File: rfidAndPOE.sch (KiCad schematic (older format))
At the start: 0 parts

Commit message: Added a few more components to the library and got about halfway done with the PoE power supply section.
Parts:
- added C1: 0.1uF, 100V, X7R, symbol C
- added C2: 1uF, 100V, symbol C
- added C3: 68pF, 200V, symbol C
- added C4: 4.7uF, 10V, symbol C
- added C5: 4.7uF, 100v, symbol CP1
- added D2: SMAJ58A, symbol DIODESCH
- added D3: BAS516, symbol DIODE
- added D5: 1N5237B, 8.2V, symbol DIODESCH
- added D? (x2): CDNBS04-B08200, symbol CDNBS04-B08200
- added L1: 3.3uH, symbol INDUCTOR
- added Q1: Si3440DV, NFET, symbol MOSFET_N
- added Q2: MMBTA42, symbol NPN
- added R2, R3: 220K, symbol R
- added R4, R400: 0.250R, symbol R
- added R5: 4.7K, symbol R
- added R6: 510R, symbol R
- added R7: 100R, 1/8W, symbol R
- added T?: PA1134, symbol PA1134
- added U?: LTC4267-3, symbol LTC4267-3
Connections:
- net labels added: GNDA
- wire segments 0 -> 61
- no-connect marks 0 -> 1

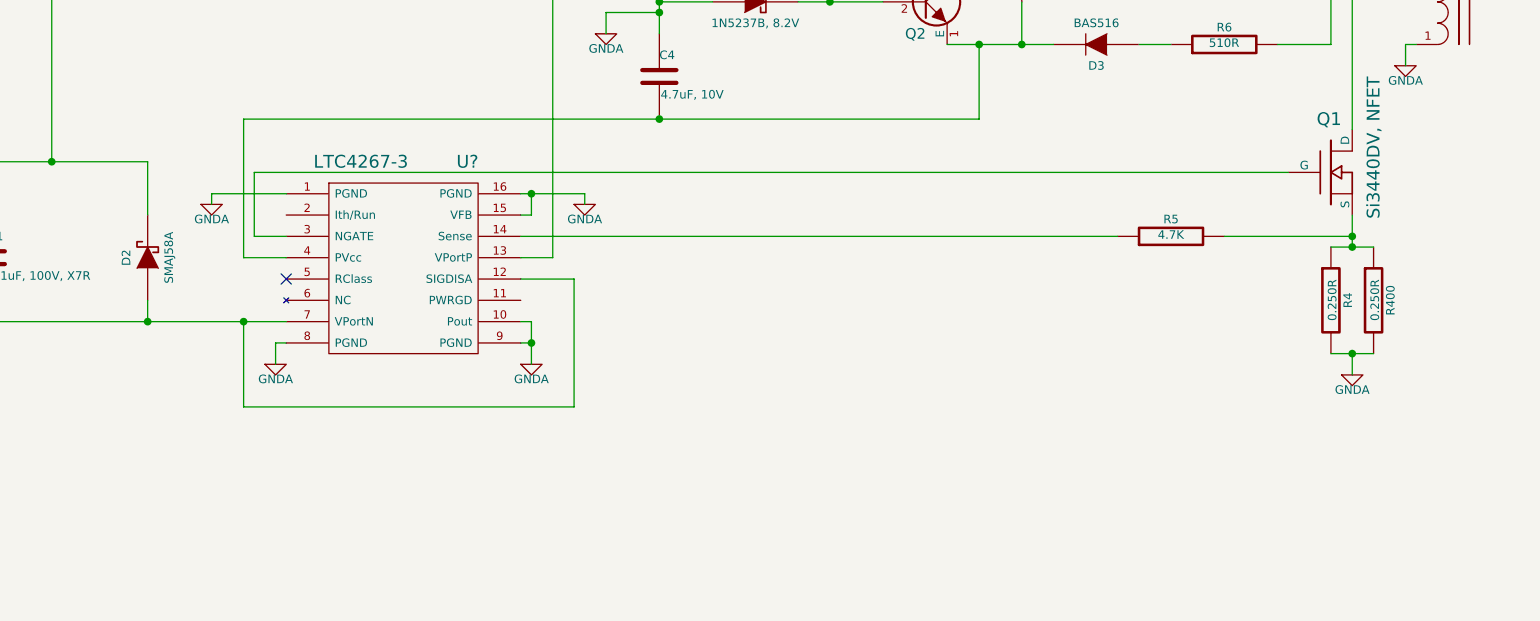
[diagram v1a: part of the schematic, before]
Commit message: PoE schematic done up to the isolation point.
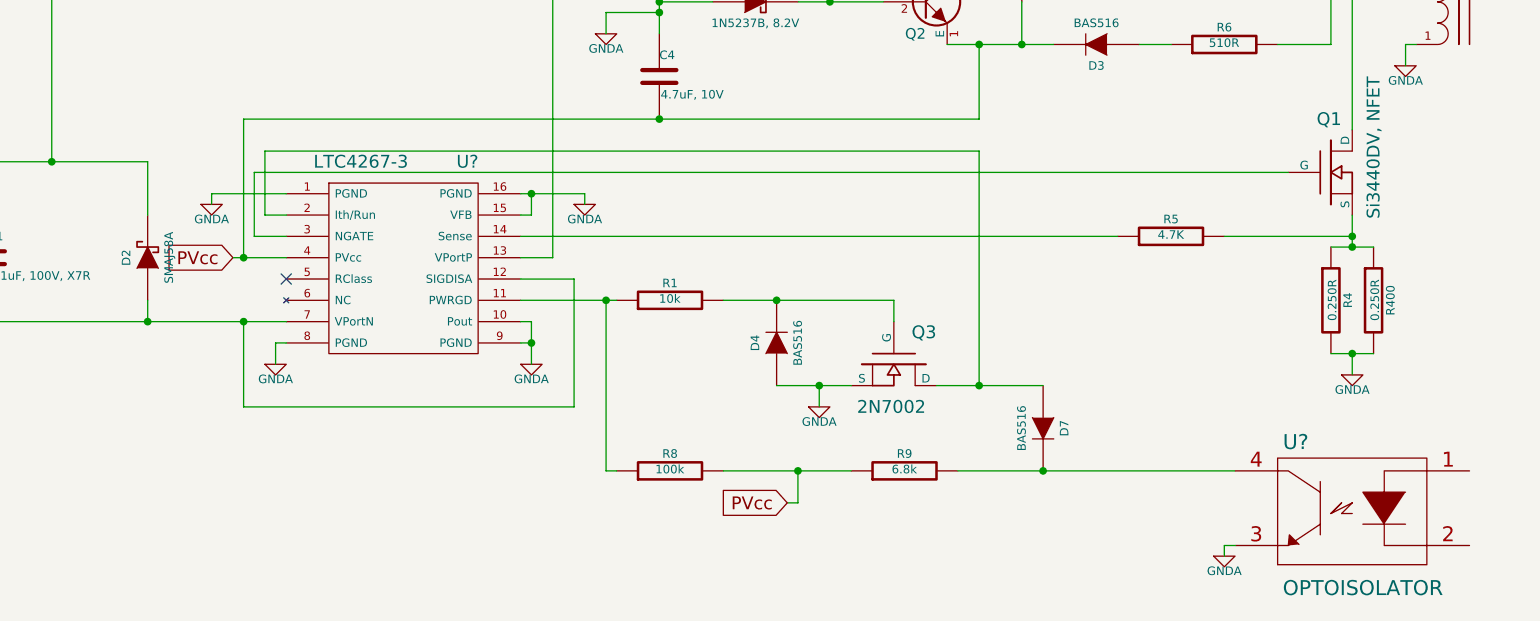
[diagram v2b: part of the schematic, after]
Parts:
- added D4, D7: BAS516, symbol DIODE
- added Q3: 2N7002, symbol MOSFET_N
- added R1: 10k, symbol R
- added R8: 100k, symbol R
- added R9: 6.8k, symbol R
- added U?: OPTOISOLATOR, symbol OPTOISOLATOR
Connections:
- net labels added: PVcc
- wire segments 61 -> 79
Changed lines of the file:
@@
 LIBS:valves
 LIBS:rfid
+LIBS:rfidAndPOE-cache
 EELAYER 24 0
 EELAYER END
@@
 	5400 3900 5400 4550
 Wire Wire Line
-	5400 4550 5600 4550
+	5350 4550 5600 4550
 $Comp
 L DIODESCH D5
@@
 	5250 4250 5600 4250
 NoConn ~ 5600 4650
+$Comp
+L MOSFET_N Q3
+U 1 1 529FE736
+P 8450 5050
+F 0 "Q3" V 8300 5250 60  0000 R CNN
+F 1 "2N7002" V 8650 5200 60  0000 R CNN
+F 2 "" H 8450 5050 60  0000 C CNN
+F 3 "" H 8450 5050 60  0000 C CNN
+	1    8450 5050
+	0    1    1    0
+$EndComp
+$Comp
+L DIODE D7
+U 1 1 529FE790
+P 9150 5350
+F 0 "D7" H 9150 5450 40  0000 C CNN
+F 1 "BAS516" H 9150 5250 40  0000 C CNN
+F 2 "" H 9150 5350 60  0000 C CNN
+F 3 "" H 9150 5350 60  0000 C CNN
+	1    9150 5350
+	0    1    1    0
+$EndComp
+$Comp
+L DIODE D4
+U 1 1 529FE7EB
+P 7900 4950
+F 0 "D4" H 7900 5050 40  0000 C CNN
+F 1 "BAS516" H 7900 4850 40  0000 C CNN
+F 2 "" H 7900 4950 60  0000 C CNN
+F 3 "" H 7900 4950 60  0000 C CNN
+	1    7900 4950
+	0    -1   -1   0
+$EndComp
+Wire Wire Line
+	8450 4750 8450 4850
+Wire Wire Line
+	7650 4750 8450 4750
+Wire Wire Line
+	7900 5150 8250 5150
+$Comp
+L GNDA #PWR?
+U 1 1 529FE8B5
+P 8100 5250
+F 0 "#PWR?" H 8100 5250 40  0001 C CNN
+F 1 "GNDA" H 8100 5180 40  0000 C CNN
+F 2 "" H 8100 5250 60  0000 C CNN
+F 3 "" H 8100 5250 60  0000 C CNN
+	1    8100 5250
+	1    0    0    -1
+$EndComp
+Wire Wire Line
+	8100 5150 8100 5250
+Connection ~ 8100 5150
+$Comp
+L R R1
+U 1 1 529FE931
+P 7400 4750
+F 0 "R1" V 7480 4750 40  0000 C CNN
+F 1 "10k" V 7407 4751 40  0000 C CNN
+F 2 "" V 7330 4750 30  0000 C CNN
+F 3 "" H 7400 4750 30  0000 C CNN
+	1    7400 4750
+	0    -1   -1   0
+$EndComp
+$Comp
+L R R8
+U 1 1 529FE945
+P 7400 5550
+F 0 "R8" V 7480 5550 40  0000 C CNN
+F 1 "100k" V 7407 5551 40  0000 C CNN
+F 2 "" V 7330 5550 30  0000 C CNN
+F 3 "" H 7400 5550 30  0000 C CNN
+	1    7400 5550
+	0    -1   -1   0
+$EndComp
+$Comp
+L R R9
+U 1 1 529FE959
+P 8500 5550
+F 0 "R9" V 8580 5550 40  0000 C CNN
+F 1 "6.8k" V 8507 5551 40  0000 C CNN
+F 2 "" V 8430 5550 30  0000 C CNN
+F 3 "" H 8500 5550 30  0000 C CNN
+	1    8500 5550
+	0    -1   -1   0
+$EndComp
+Wire Wire Line
+	6700 4750 7150 4750
+Connection ~ 7900 4750
+Wire Wire Line
+	7100 4750 7100 5550
+Wire Wire Line
+	7100 5550 7150 5550
+Connection ~ 7100 4750
+Wire Wire Line
+	7650 5550 8250 5550
+Wire Wire Line
+	8750 5550 10050 5550
+Wire Wire Line
+	8650 5150 9150 5150
+Wire Wire Line
+	5600 4350 5500 4350
+Wire Wire Line
+	5500 4350 5500 4050
+Wire Wire Line
+	5500 4050 8850 4050
+Wire Wire Line
+	8850 4050 8850 5150
+Connection ~ 8850 5150
+Text GLabel 5350 4550 0    60   Input ~ 0
+PVcc
+Text GLabel 7950 5700 0    60   Input ~ 0
+PVcc
+Wire Wire Line
+	7950 5700 8000 5700
+Wire Wire Line
+	8000 5700 8000 5550
+Connection ~ 8000 5550
+Connection ~ 5400 4550
+$Comp
+L OPTOISOLATOR U?
+U 1 1 529FF254
+P 10000 5750
+F 0 "U?" H 10335 6085 70  0000 C CNN
+F 1 "OPTOISOLATOR" H 10650 5400 70  0000 C CNN
+F 2 "" H 10600 5750 60  0000 C CNN
+F 3 "" H 10600 5750 60  0000 C CNN
+	1    10000 5750
+	1    0    0    -1
+$EndComp
+Connection ~ 9150 5550
+$Comp
+L GNDA #PWR?
+U 1 1 529FF2D9
+P 10000 5950
+F 0 "#PWR?" H 10000 5950 40  0001 C CNN
+F 1 "GNDA" H 10000 5880 40  0000 C CNN
+F 2 "" H 10000 5950 60  0000 C CNN
+F 3 "" H 10000 5950 60  0000 C CNN
+	1    10000 5950
+	1    0    0    -1
+$EndComp
+Wire Wire Line
+	10050 5900 10000 5900
+Wire Wire Line
+	10000 5900 10000 5950
 $EndSCHEMATC

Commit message: Placed all of the components for the 5V isolated output from PoE.
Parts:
- added C14, C?: 100uF, 6.3V, X5R, symbol C
- added C6: 470pF, symbol C
- added C9: 220uF, 6.3v, symbol CP1
- added C? (x4): C, symbol C
- added D1: SMB540, symbol DIODESCH
- added D?: VREF, symbol VREF
- added R10: 10R, symbol R
- added R? (x5): R, symbol R
- U?: value OPTOISOLATOR -> PS2811
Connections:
- net labels added: 5VPoE, GND
- wire segments 79 -> 93

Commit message: Finished up the output side of the PoE 5V supply.
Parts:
- C12: renamed from C?; value C -> 1uF
- C13: renamed from C?; value C -> 33nF
- C7: renamed from C?; value C -> 27nF
- C8: renamed from C?; value C -> 2.8nF, 250VAC, YCAP
- D8: renamed from D?; value VREF -> TLV431
- R11: renamed from R?; value R -> 1k
- R12: renamed from R?; value R -> 47k
- R13: renamed from R?; value R -> 100k, 1%
- R14: renamed from R?; value R -> 33.2k
- R21: renamed from R?; value R -> 470R
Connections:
- wire segments 93 -> 112
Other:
- moved on the sheet: C12, C13, C7, C8, R11, R12, R13, R14, R21
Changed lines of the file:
@@
 L GNDA #PWR?
 U 1 1 529FF2D9
-P 9905 6290
-F 0 "#PWR?" H 9905 6290 40  0001 C CNN
-F 1 "GNDA" H 9905 6220 40  0000 C CNN
-F 2 "" H 9905 6290 60  0000 C CNN
-F 3 "" H 9905 6290 60  0000 C CNN
-	1    9905 6290
+P 9905 6485
+F 0 "#PWR?" H 9905 6485 40  0001 C CNN
+F 1 "GNDA" H 9905 6415 40  0000 C CNN
+F 2 "" H 9905 6485 60  0000 C CNN
+F 3 "" H 9905 6485 60  0000 C CNN
+	1    9905 6485
 	1    0    0    -1
 $EndComp
@@
 	12170 2970 12255 2970
 Wire Wire Line
-	12800 2740 12070 2740
+	12070 2740 12800 2740
 Wire Wire Line
 	12655 2970 12770 2970
 Wire Wire Line
-	12770 3225 12770 2740
+	12770 2740 12770 4795
 Connection ~ 12770 2740
-Connection ~ 12770 2970
-Wire Wire Line
-	11865 3225 12770 3225
+Wire Wire Line
+	12770 3225 11865 3225
 Connection ~ 12570 3225
 Connection ~ 12245 3225
@@
 Connection ~ 12290 3625
 $Comp
-L R R?
+L R R14
 U 1 1 52A00B47
-P 12790 5990
-F 0 "R?" V 12870 5990 40  0000 C CNN
-F 1 "R" V 12797 5991 40  0000 C CNN
-F 2 "" V 12720 5990 30  0000 C CNN
-F 3 "" H 12790 5990 30  0000 C CNN
-	1    12790 5990
-	1    0    0    -1
-$EndComp
-Wire Wire Line
-	9905 5900 9905 6290
-$Comp
-L R R?
+P 12770 6100
+F 0 "R14" V 12850 6100 40  0000 C CNN
+F 1 "33.2k" V 12777 6101 40  0000 C CNN
+F 2 "" V 12700 6100 30  0000 C CNN
+F 3 "" H 12770 6100 30  0000 C CNN
+	1    12770 6100
+	1    0    0    -1
+$EndComp
+Wire Wire Line
+	9905 5900 9905 6485
+$Comp
+L R R13
 U 1 1 52A00D13
-P 12790 4795
-F 0 "R?" V 12870 4795 40  0000 C CNN
-F 1 "R" V 12797 4796 40  0000 C CNN
-F 2 "" V 12720 4795 30  0000 C CNN
-F 3 "" H 12790 4795 30  0000 C CNN
-	1    12790 4795
-	1    0    0    -1
-$EndComp
-$Comp
-L R R?
+P 12770 5045
+F 0 "R13" V 12850 5045 40  0000 C CNN
+F 1 "100k, 1%" V 12777 5046 40  0000 C CNN
+F 2 "" V 12700 5045 30  0000 C CNN
+F 3 "" H 12770 5045 30  0000 C CNN
+	1    12770 5045
+	1    0    0    -1
+$EndComp
+$Comp
+L R R21
 U 1 1 52A00D3B
-P 12375 4300
-F 0 "R?" V 12455 4300 40  0000 C CNN
-F 1 "R" V 12382 4301 40  0000 C CNN
-F 2 "" V 12305 4300 30  0000 C CNN
-F 3 "" H 12375 4300 30  0000 C CNN
-	1    12375 4300
+P 12300 4500
+F 0 "R21" V 12380 4500 40  0000 C CNN
+F 1 "470R" V 12307 4501 40  0000 C CNN
+F 2 "" V 12230 4500 30  0000 C CNN
+F 3 "" H 12300 4500 30  0000 C CNN
+	1    12300 4500
 	0    -1   -1   0
 $EndComp
 $Comp
-L R R?
+L R R11
 U 1 1 52A00D4F
-P 11795 4725
-F 0 "R?" V 11875 4725 40  0000 C CNN
-F 1 "R" V 11802 4726 40  0000 C CNN
-F 2 "" V 11725 4725 30  0000 C CNN
-F 3 "" H 11795 4725 30  0000 C CNN
-	1    11795 4725
-	1    0    0    -1
-$EndComp
-$Comp
-L C C?
+P 11400 4750
+F 0 "R11" V 11480 4750 40  0000 C CNN
+F 1 "1k" V 11407 4751 40  0000 C CNN
+F 2 "" V 11330 4750 30  0000 C CNN
+F 3 "" H 11400 4750 30  0000 C CNN
+	1    11400 4750
+	1    0    0    -1
+$EndComp
+$Comp
+L C C12
 U 1 1 52A00D63
-P 11350 4710
-F 0 "C?" H 11350 4810 40  0000 L CNN
-F 1 "C" H 11356 4625 40  0000 L CNN
-F 2 "" H 11388 4560 30  0000 C CNN
-F 3 "" H 11350 4710 60  0000 C CNN
-	1    11350 4710
-	1    0    0    -1
-$EndComp
-$Comp
-L C C?
+P 11100 4700
+F 0 "C12" H 11100 4800 40  0000 L CNN
+F 1 "1uF" H 11106 4615 40  0000 L CNN
+F 2 "" H 11138 4550 30  0000 C CNN
+F 3 "" H 11100 4700 60  0000 C CNN
+	1    11100 4700
+	1    0    0    -1
+$EndComp
+$Comp
+L C C13
 U 1 1 52A00D77
-P 12095 4710
-F 0 "C?" H 12095 4810 40  0000 L CNN
-F 1 "C" H 12101 4625 40  0000 L CNN
-F 2 "" H 12133 4560 30  0000 C CNN
-F 3 "" H 12095 4710 60  0000 C CNN
-	1    12095 4710
-	1    0    0    -1
-$EndComp
-$Comp
-L C C?
+P 11650 4700
+F 0 "C13" H 11650 4800 40  0000 L CNN
+F 1 "33nF" H 11656 4615 40  0000 L CNN
+F 2 "" H 11688 4550 30  0000 C CNN
+F 3 "" H 11650 4700 60  0000 C CNN
+	1    11650 4700
+	1    0    0    -1
+$EndComp
+$Comp
+L C C7
 U 1 1 52A00D8B
-P 12100 5765
-F 0 "C?" H 12100 5865 40  0000 L CNN
-F 1 "C" H 12106 5680 40  0000 L CNN
-F 2 "" H 12138 5615 30  0000 C CNN
-F 3 "" H 12100 5765 60  0000 C CNN
-	1    12100 5765
-	1    0    0    -1
-$EndComp
-$Comp
-L R R?
+P 11600 5610
+F 0 "C7" H 11600 5710 40  0000 L CNN
+F 1 "27nF" H 11606 5525 40  0000 L CNN
+F 2 "" H 11638 5460 30  0000 C CNN
+F 3 "" H 11600 5610 60  0000 C CNN
+	1    11600 5610
+	1    0    0    -1
+$EndComp
+$Comp
+L R R12
 U 1 1 52A00DA9
-P 12415 5420
-F 0 "R?" V 12495 5420 40  0000 C CNN
-F 1 "R" V 12422 5421 40  0000 C CNN
-F 2 "" V 12345 5420 30  0000 C CNN
-F 3 "" H 12415 5420 30  0000 C CNN
-	1    12415 5420
+P 12150 5410
+F 0 "R12" V 12230 5410 40  0000 C CNN
+F 1 "47k" V 12157 5411 40  0000 C CNN
+F 2 "" V 12080 5410 30  0000 C CNN
+F 3 "" H 12150 5410 30  0000 C CNN
+	1    12150 5410
 	0    -1   -1   0
 $EndComp
 $Comp
-L C C?
+L C C8
 U 1 1 52A00DCC
-P 11200 6365
-F 0 "C?" H 11200 6465 40  0000 L CNN
-F 1 "C" H 11206 6280 40  0000 L CNN
-F 2 "" H 11238 6215 30  0000 C CNN
-F 3 "" H 11200 6365 60  0000 C CNN
-	1    11200 6365
+P 10620 6350
+F 0 "C8" V 10685 6440 40  0000 L CNN
+F 1 "2.8nF, 250VAC, YCAP" V 10475 6030 40  0000 L CNN
+F 2 "" H 10658 6200 30  0000 C CNN
+F 3 "" H 10620 6350 60  0000 C CNN
+	1    10620 6350
 	0    -1   -1   0
 $EndComp
 $Comp
-L VREF D?
+L VREF D8
 U 1 1 52A00EE8
-P 12100 6230
-F 0 "D?" H 11975 6265 40  0000 C CNN
-F 1 "VREF" H 11965 6190 40  0000 C CNN
-F 2 "" V 12100 6240 60  0000 C CNN
-F 3 "" V 12100 6240 60  0000 C CNN
-	1    12100 6230
-	1    0    0    -1
-$EndComp
+P 11600 6230
+F 0 "D8" H 11475 6265 40  0000 C CNN
+F 1 "TLV431" H 11465 6190 40  0000 C CNN
+F 2 "" V 11600 6240 60  0000 C CNN
+F 3 "" V 11600 6240 60  0000 C CNN
+	1    11600 6230
+	1    0    0    -1
+$EndComp
+$Comp
+L GND #PWR?
+U 1 1 52A252C8
+P 12770 6490
+F 0 "#PWR?" H 12770 6490 30  0001 C CNN
+F 1 "GND" H 12770 6420 30  0001 C CNN
+F 2 "" H 12770 6490 60  0000 C CNN
+F 3 "" H 12770 6490 60  0000 C CNN
+	1    12770 6490
+	1    0    0    -1
+$EndComp
+Wire Wire Line
+	10420 6350 9905 6350
+Connection ~ 9905 6350
+Wire Wire Line
+	10825 6350 12770 6350
+Connection ~ 12770 2970
+Connection ~ 12770 3225
+Connection ~ 11600 6350
+Wire Wire Line
+	12770 5295 12770 5850
+Wire Wire Line
+	12770 6350 12770 6490
+Wire Wire Line
+	11600 5810 11600 6090
+Wire Wire Line
+	11710 6230 11905 6230
+Wire Wire Line
+	11905 6230 11905 5770
+Wire Wire Line
+	11905 5770 12770 5770
+Connection ~ 12770 5770
+Wire Wire Line
+	11150 5900 11600 5900
+Connection ~ 11600 5900
+Wire Wire Line
+	11600 5410 11900 5410
+Wire Wire Line
+	12400 5410 12770 5410
+Connection ~ 12770 5410
+Wire Wire Line
+	11100 4500 12050 4500
+Connection ~ 11650 4500
+Connection ~ 11400 4500
+Wire Wire Line
+	11400 5000 11400 5550
+Wire Wire Line
+	11400 5550 11150 5550
+Wire Wire Line
+	11650 4900 11650 5100
+Wire Wire Line
+	11650 5100 11400 5100
+Connection ~ 11400 5100
+$Comp
+L GND #PWR?
+U 1 1 52A263CC
+P 11100 5000
+F 0 "#PWR?" H 11100 5000 30  0001 C CNN
+F 1 "GND" H 11100 4930 30  0001 C CNN
+F 2 "" H 11100 5000 60  0000 C CNN
+F 3 "" H 11100 5000 60  0000 C CNN
+	1    11100 5000
+	1    0    0    -1
+$EndComp
+Wire Wire Line
+	11100 4900 11100 5000
+Wire Wire Line
+	12550 4500 12770 4500
+Wire Wire Line
+	12770 4500 12770 4495
+Connection ~ 12770 4495
 $EndSCHEMATC

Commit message: Swapped out the bridge rectifier symbol on the schematic for one that is a normal size.
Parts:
- removed D? (x2): CDNBS04-B08200, symbol CDNBS04-B08200
- added D? (x2): CDNBS04-B08200, symbol BRIDGE_RECTIFIER

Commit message: Added several test points for the PoE power supply. Also added a 5V test LED and a note about the isolated ground.
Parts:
- added D?: LED, symbol LED
- added P?: +5V, symbol TST
- added P?: GND, symbol TST
- added P?: PoE+, symbol TST
- added P?: PoE-, symbol TST
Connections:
- wire segments 112 -> 114
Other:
- note added: "Note: GNDA is from ethernet. \nGND on the rest of the circuit is\nisolated from this."
- moved on the sheet: C1, C12, C13, C14, C2, C3, C4, C5, C6, C7, C8, C9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

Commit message: Forgot a current limiting resistor for the 5V test/power good LED. :)
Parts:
- added R?: 2.8k, symbol RESISTOR
- D?: value LED -> 5V LED
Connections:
- wire segments 114 -> 115
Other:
- moved on the sheet: D?
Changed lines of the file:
@@
 L LED D?
 U 1 1 52A27A6E
-P 13790 1215
-F 0 "D?" H 13790 1315 50  0000 C CNN
-F 1 "LED" H 13790 1115 50  0000 C CNN
-F 2 "" H 13790 1215 60  0000 C CNN
-F 3 "" H 13790 1215 60  0000 C CNN
-	1    13790 1215
+P 13790 1690
+F 0 "D?" H 13790 1790 50  0000 C CNN
+F 1 "5V LED" H 13795 1575 50  0000 C CNN
+F 2 "" H 13790 1690 60  0000 C CNN
+F 3 "" H 13790 1690 60  0000 C CNN
+	1    13790 1690
 	0    1    1    0
 $EndComp
 Wire Wire Line
-	13790 1015 13790 930
+	13790 930  13790 1060
 Connection ~ 13790 930
 $Comp
 L GND #PWR?
 U 1 1 52A27D1F
-P 13790 1480
-F 0 "#PWR?" H 13790 1480 30  0001 C CNN
-F 1 "GND" H 13790 1410 30  0001 C CNN
-F 2 "" H 13790 1480 60  0000 C CNN
-F 3 "" H 13790 1480 60  0000 C CNN
-	1    13790 1480
+P 13790 1955
+F 0 "#PWR?" H 13790 1955 30  0001 C CNN
+F 1 "GND" H 13790 1885 30  0001 C CNN
+F 2 "" H 13790 1955 60  0000 C CNN
+F 3 "" H 13790 1955 60  0000 C CNN
+	1    13790 1955
 	1    0    0    -1
 $EndComp
 Wire Wire Line
-	13790 1415 13790 1480
+	13790 1890 13790 1955
+$Comp
+L RESISTOR R?
+U 1 1 52A27F11
+P 13790 1240
+F 0 "R?" V 13870 1240 40  0000 C CNN
+F 1 "2.8k" V 13700 1245 40  0000 C CNN
+F 2 "" V 13720 1240 30  0000 C CNN
+F 3 "" H 13790 1240 30  0000 C CNN
+	1    13790 1240
+	1    0    0    -1
+$EndComp
+Wire Wire Line
+	13790 1490 13790 1420
 $EndSCHEMATC
